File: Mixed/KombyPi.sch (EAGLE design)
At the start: 15 parts, among them IC3 DS1307, J1 POWER_JACKPTH, J2 MOLEX-39501XXX4, Q1 32.768

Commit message: Update KombyPi mixed boards to be cleaner layout.
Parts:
- removed BAT: CR1220, adafruit:CR1220THM
- removed C1: 0.1uF, adafruit:C-US025-025X050
- removed IC3: DS1307, adafruit:DS1307
- removed JP3: RASPBERRYPI-B+-GPIO, SparkFun-Boards:RASPBERRYPI-B+-GPIO
- removed Q1: 32.768, crystal:CRYTALTC38H
- added JP1: RASPBERRYPI-GPIOPTH, SparkFun-Boards:RASPBERRYPI-GPIOPTH
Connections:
- removed net N$14: IC3.X1, Q1.2
- removed net N$15: IC3.X2, Q1.1
- removed net N$39: BAT.+1, IC3.VBAT
- removed net SQW: IC3.SQW/OUT
- new net WS2801_VCC_FUSED: F2.1, J2.4
- net 3.3V: now also JP1.3.3V@17; no longer JP3.3.3V@17
- net CE0: now also JP1.CE0; no longer JP3.CE0
- net CE1: now also JP1.CE1; no longer JP3.CE1
- net GND: now also JP1.GND@14, JP1.GND@20, JP1.GND@25, JP1.GND@6, JP1.GND@9; no longer BAT.-, C1.2, IC3.GND, JP3.GND@14, JP3.GND@20, JP3.GND@25, JP3.GND@30, JP3.GND@34, JP3.GND@39, JP3.GND@6, JP3.GND@9
- net MISO: now also JP1.MISO; no longer JP3.MISO
- net MOSI: now also JP1.MOSI; no longer JP3.MOSI
- net RF_CE: now also JP1.GP22; no longer JP3.GP22
- net RXI: now also JP1.RXI; no longer JP3.RXI
- net SCL: now also JP1.SCL; no longer IC3.SCL, JP3.SCL
- net SCLK: now also JP1.SCLK; no longer JP3.SCLK
- net SDA: now also JP1.SDA; no longer IC3.SDA, JP3.SDA
- net TXO: now also JP1.TXO; no longer JP3.TXO
- net VCC: now also JP1.5V@2, JP1.5V@4; no longer C1.1, D1.C, F2.2, IC3.VCC, JP3.5V@2, JP3.5V@4
- net WS2801_VCC: now also D1.C, F2.2; no longer F2.1, J2.4
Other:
- note removed: "RTC"
- moved on the sheet: C2, C3, C4, D1, F2, FTDI, J2, JP4, V1/+UB, V1/-UB, V1/1, V1/2

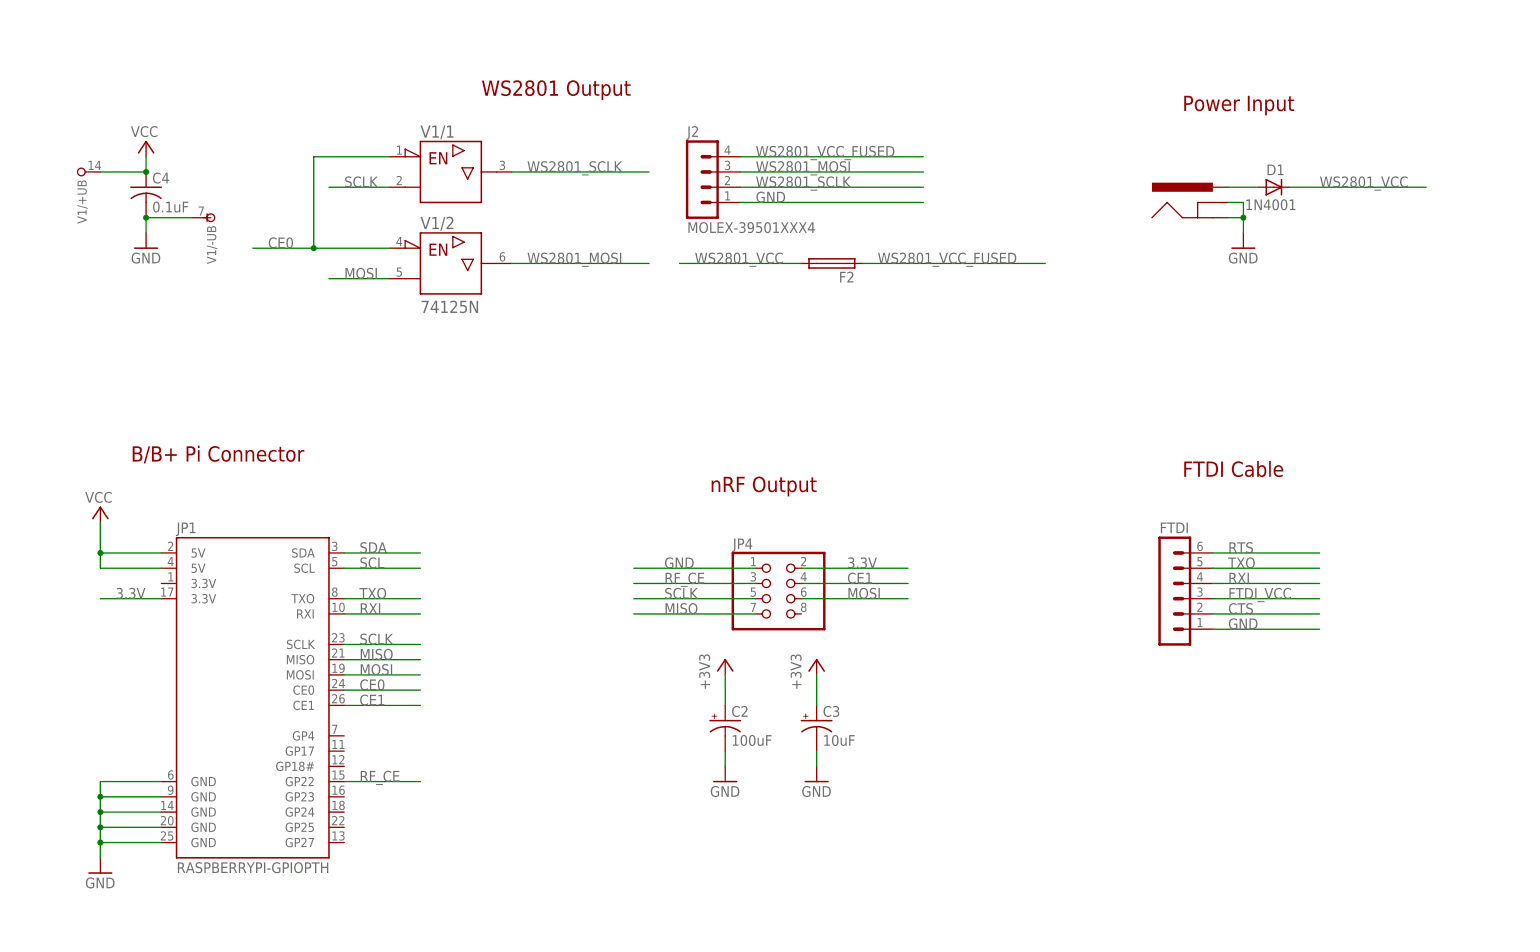
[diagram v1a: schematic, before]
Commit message: Update KombyPi to have proper orientation for nRF
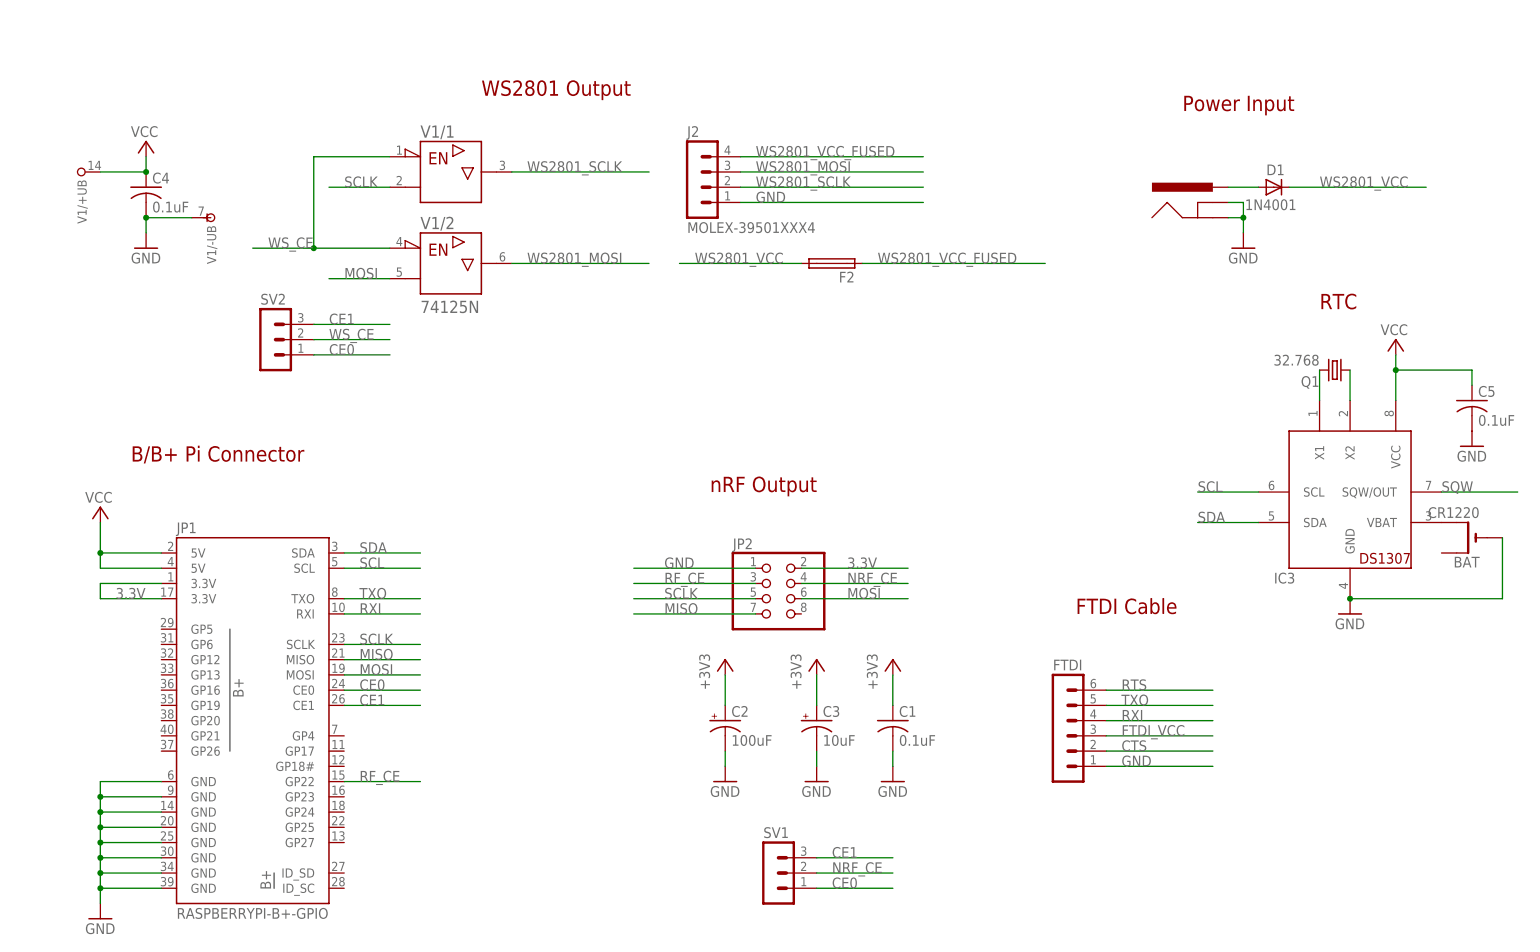
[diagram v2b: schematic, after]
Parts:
- removed JP4: (no value), adafruit:PINHD-2X4
- added BAT: CR1220, adafruit:CR1220THM
- added C1, C5: 0.1uF, adafruit:C-US025-025X050
- added IC3: DS1307, adafruit:DS1307
- added JP2: (no value), Materdaddy-Custom:NRF_HEADER
- added Q1: 32.768, crystal:CRYTALTC38H
- added SV1, SV2: (no value), Materdaddy-Custom:MA03-1
- FTDI: device con-lstb:MA06-1 -> Materdaddy-Custom:MA06-1
- JP1: value RASPBERRYPI-GPIOPTH -> RASPBERRYPI-B+-GPIO; device SparkFun-Boards:RASPBERRYPI-GPIOPTH -> SparkFun-Boards:RASPBERRYPI-B+-GPIO
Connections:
- new net +3V3: C1.1
- new net N$14: IC3.X1, Q1.2
- new net N$15: IC3.X2, Q1.1
- new net N$39: BAT.+1, IC3.VBAT
- new net NRF_CE: JP2.CSN, SV1.2
- new net SQW: IC3.SQW/OUT
- new net WS_CE: SV2.2, V1/1.!G, V1/2.!G
- net 3.3V: now also JP1.3.3V@1, JP2.VCC; no longer JP4.2
- net CE0: now also SV1.1, SV2.1; no longer V1/1.!G, V1/2.!G
- net CE1: now also SV1.3, SV2.3; no longer JP4.4
- net GND: now also BAT.-, C1.2, C5.2, IC3.GND, JP1.GND@30, JP1.GND@34, JP1.GND@39, JP2.GND; no longer JP4.1
- net MISO: now also JP2.MISO; no longer JP4.7
- net MOSI: now also JP2.MOSI; no longer JP4.6
- net RF_CE: now also JP2.CE; no longer JP4.3
- net SCL: now also IC3.SCL
- net SCLK: now also JP2.SCK; no longer JP4.5
- net SDA: now also IC3.SDA
- net VCC: now also C5.1, IC3.VCC
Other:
- note added: "RTC"
- moved on the sheet: FTDI
